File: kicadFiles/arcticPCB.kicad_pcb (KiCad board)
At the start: 2 copper layers, 283 x 94.2 mm, 175 parts, among them J1 TYPE-C-31-M12_13, J2 Conn_01x14, J3 Conn_ARM_JTAG_SWD_10, SW1 ESC, SW10 0, SW11 -_, SW12 =+, SW13 LBKSP, SW14 2U BKSP, SW15 TAB_150, SW16 Q, SW17 W, SW18 E, SW19 R, SW2 1, SW20 T, SW21 Y, SW22 U, SW23 I, SW24 O, SW25 P, SW26 [{, SW27 ]}, SW28 \|_150, SW29 CAPS_175, SW3 2, SW30 A, SW31 S, SW32 D, SW33 F, SW34 G, SW35 H, SW36 J, SW37 K, SW38 L, SW39 :;, SW4 3, SW40 "', SW41 ENTER_225, SW42 LSHIFT_225, SW43 Z, SW44 X, SW45 C, SW46 V, SW47 B, SW48 N, SW49 M, SW5 4, SW50 <,, SW51 >., SW52 ?/, SW53 RSHIFT_275, SW54 LCTRL_150, SW55 LGUI_100, SW56 LALT_150, SW57 SPACE_7U, SW58 RALT_150, SW59 RGUI_100, SW6 5, SW60 RCTRL_150, SW61 FN_100, SW62 RSHIFT_175, SW63 STEPPED_CAPS_125, SW64 1U LBKSP, SW65 1U RBKSP, SW7 7, SW8 8, SW9 9, U1 STM32F072-LQFP48, U2 USBLC6-2SC6, U3 MCP1700-3302E_SOT23

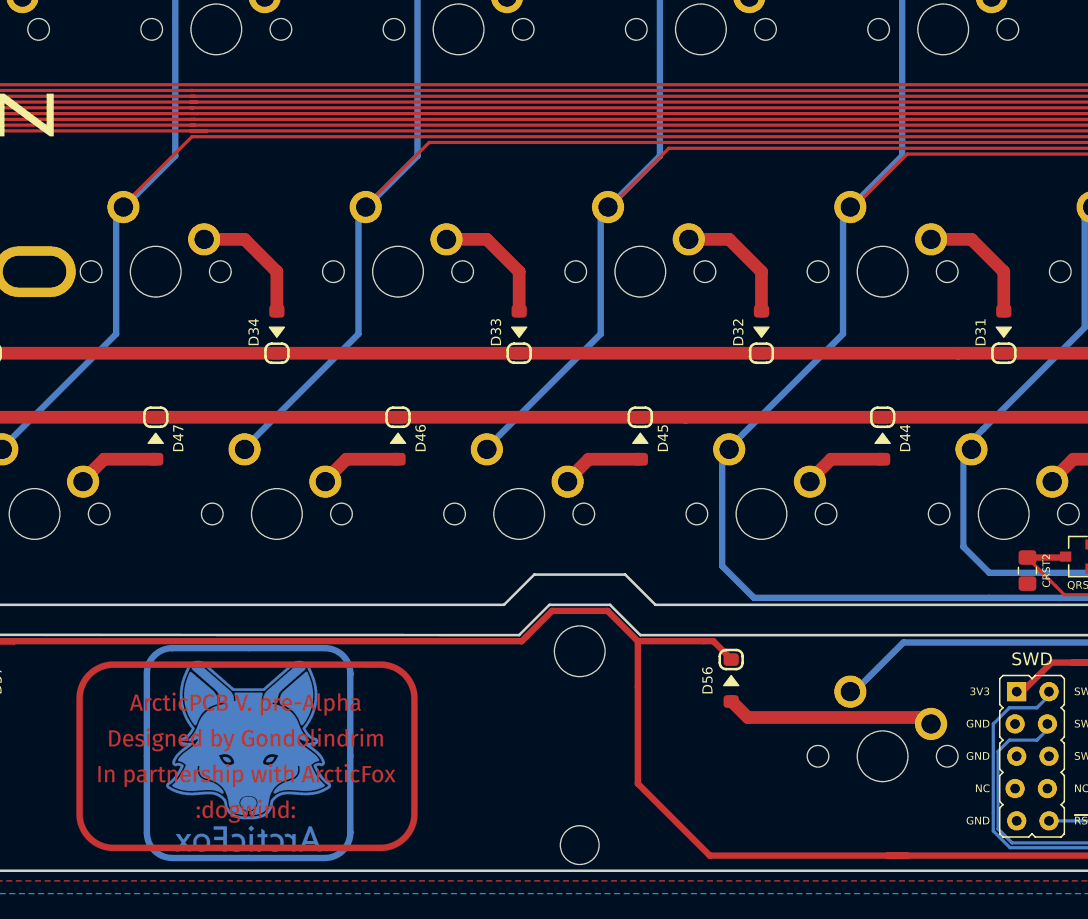
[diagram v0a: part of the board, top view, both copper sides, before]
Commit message: Initial Putain Edition support
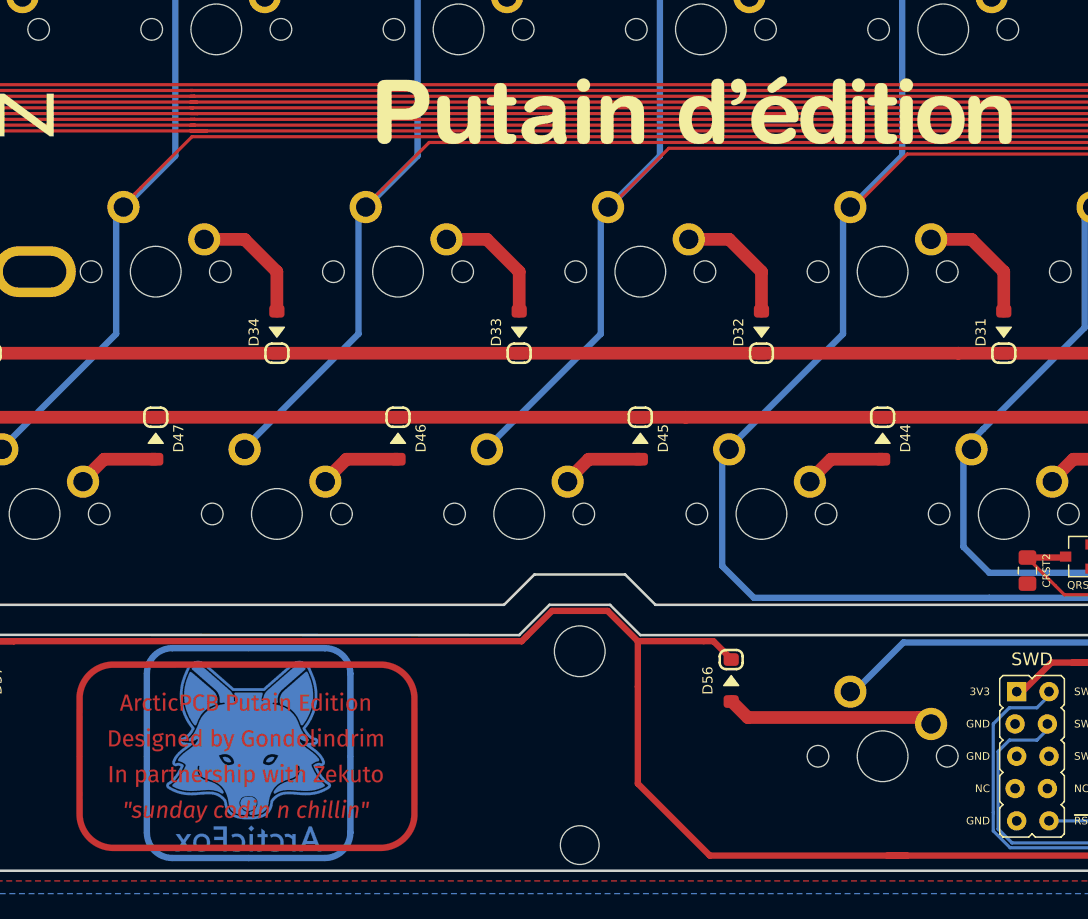
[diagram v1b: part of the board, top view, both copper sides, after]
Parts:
- added L6: Putain Logo, arcticGraphics:putainLogo_50_5, F.Cu at (279.0, 116.8)
- SW10: value 0 -> 9
- SW11: value -_ -> 0
- SW12: value =+ -> -_
- SW13: value LBKSP -> +=
- SW7: value 7 -> 6
- SW8: value 8 -> 7
- SW9: value 9 -> 8
